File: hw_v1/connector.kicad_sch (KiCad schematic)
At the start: 36 parts, among them J1 Conn_02x24_Counter_Clockwise, J12 Delphi_Sicma_24, J13 Delphi_Sicma_24, J14 Conn_01x04, Q3 FDS6890A, U11 L78M05ABDT-TR, U12 LM74800, U19 L78M05ABDT-TR

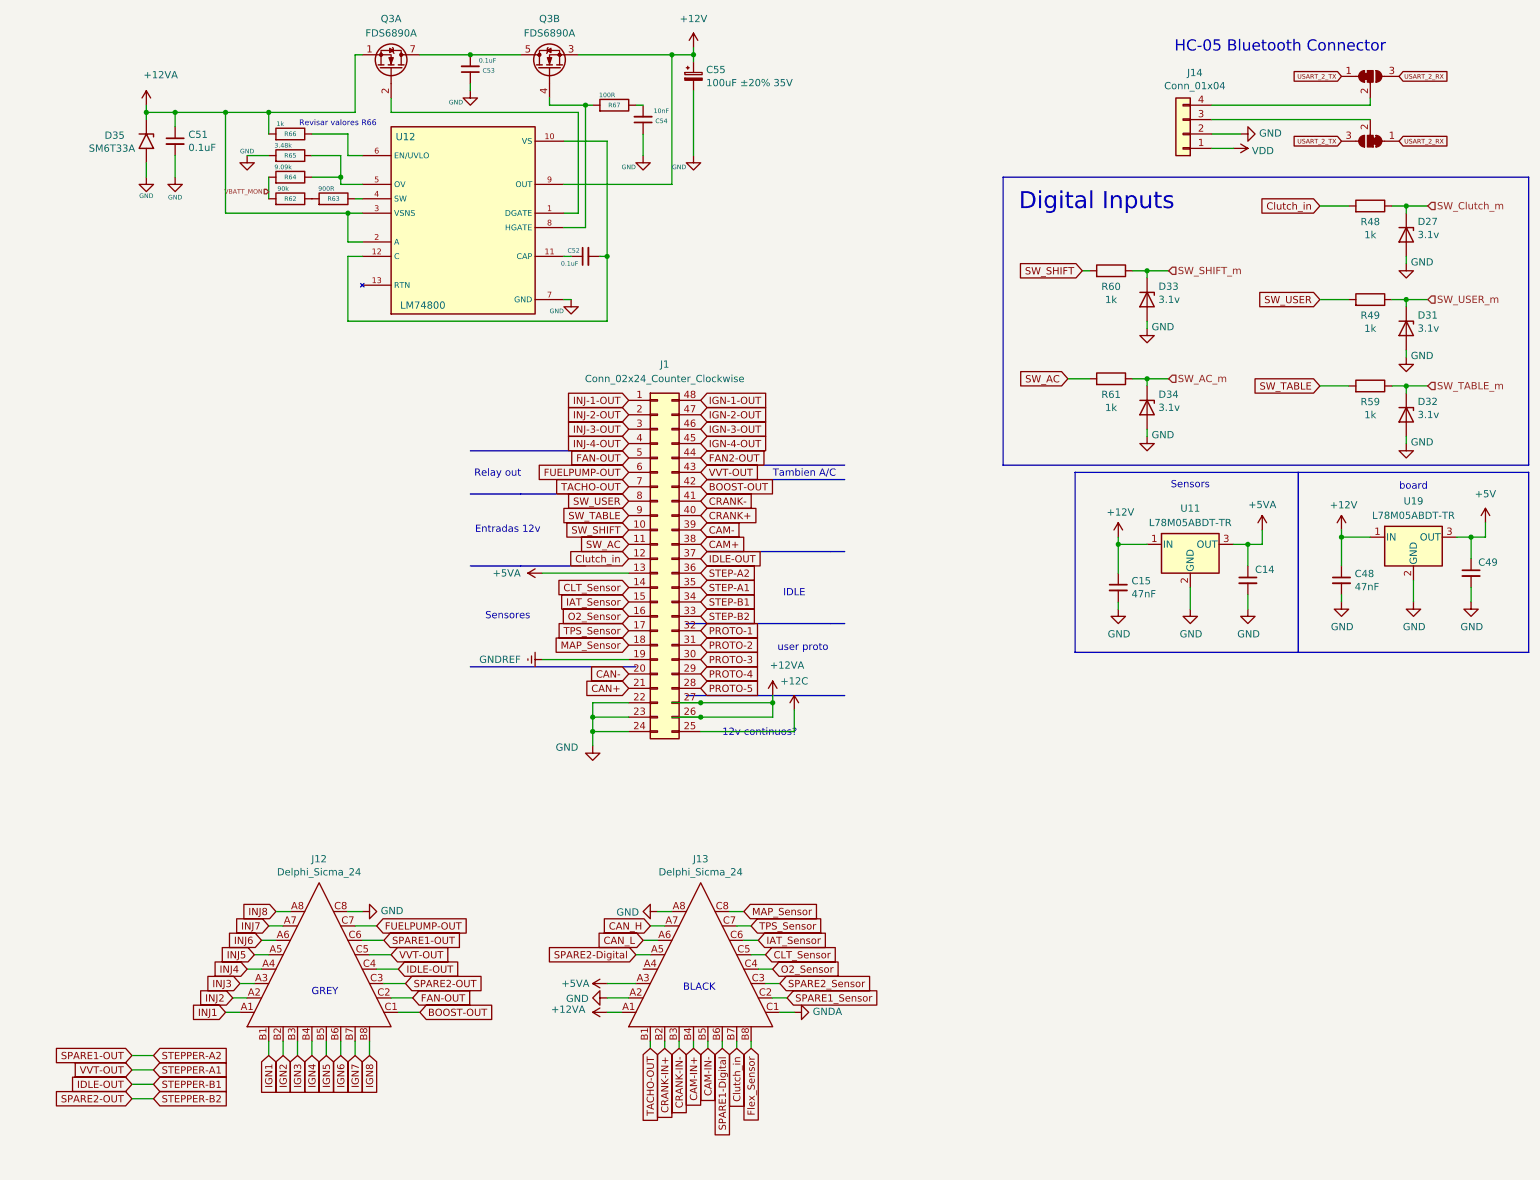
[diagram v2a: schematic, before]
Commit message: wip sensors traces, added can
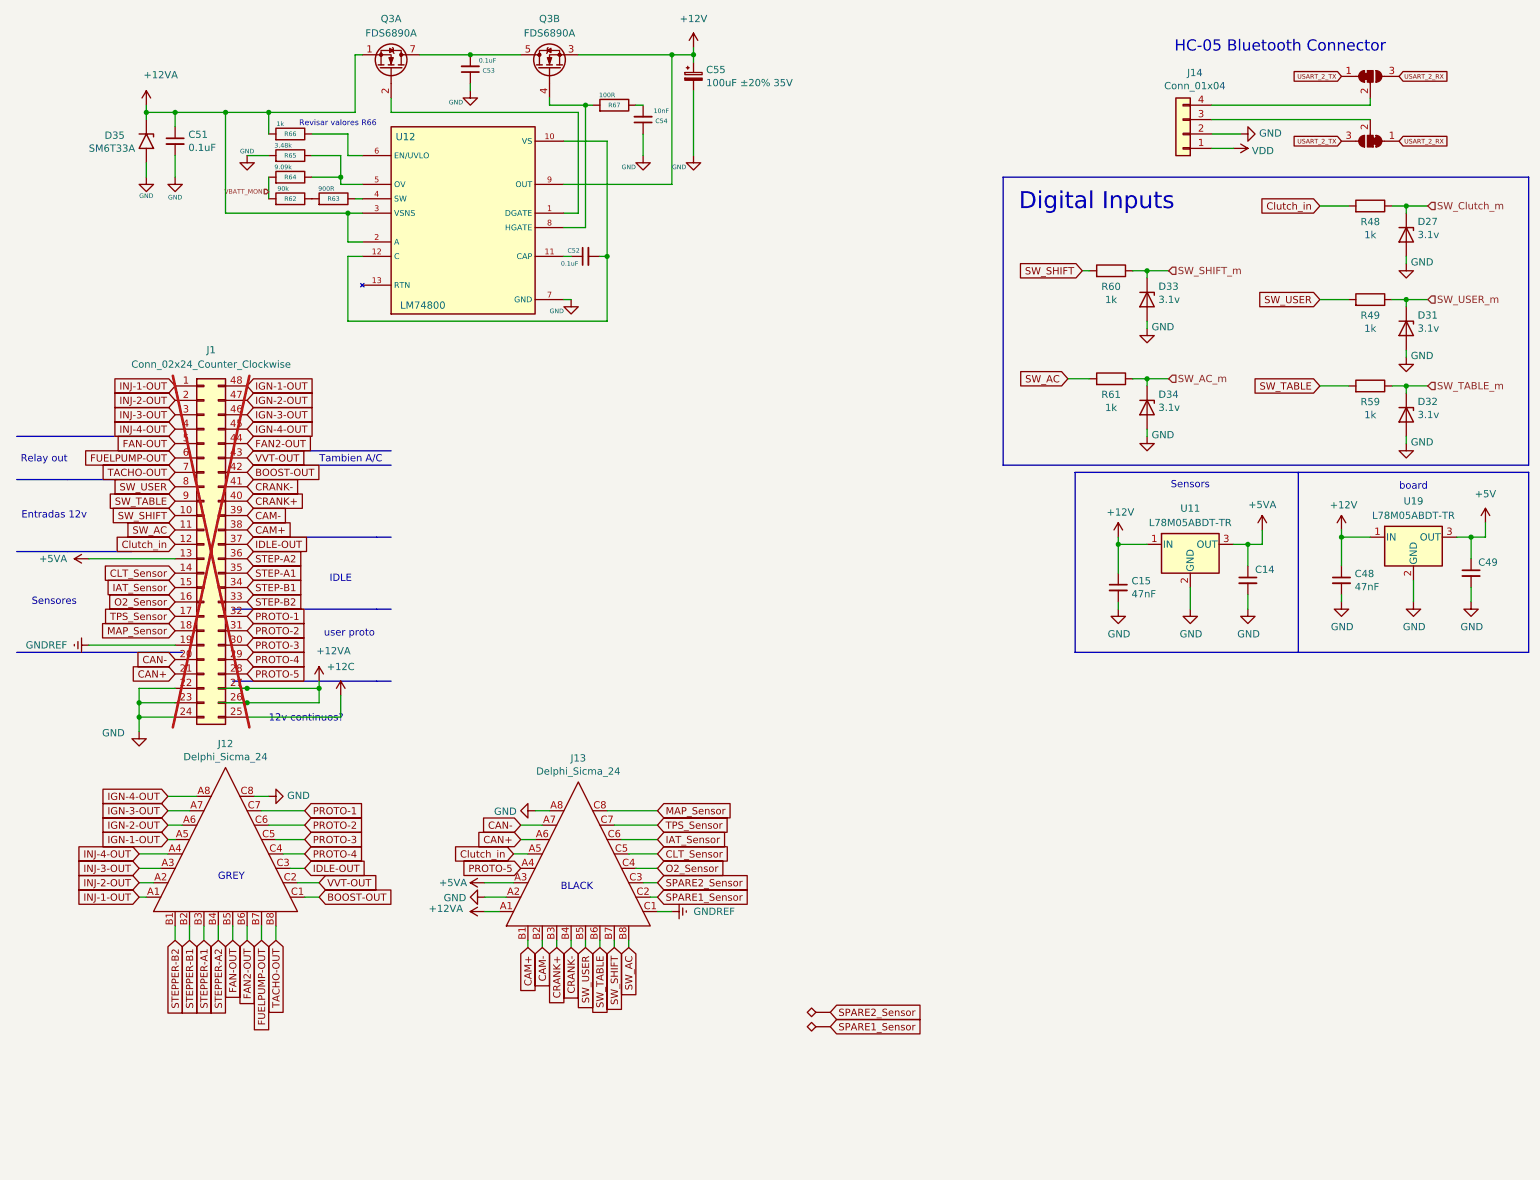
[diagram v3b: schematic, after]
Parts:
- added TP19, TP20: TestPoint_Alt, TestPoint:TestPoint_THTPad_1.0x1.0mm_Drill0.5mm, symbol Connector:TestPoint_Alt
- J1: now not fitted; now left out of the parts list
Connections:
- net CAM-IN+ is gone; now on net CRANK-: J13.B4
- net CAM-IN- is gone; now on net SW_USER: J13.B5
- net CAN_H is gone; now on net CAN-: J13.A7
- net CAN_L is gone; now on net CAN+: J13.A6
- net CRANK-IN+ is gone; now on net CAM-: J13.B2
- net CRANK-IN- is gone; now on net CRANK+: J13.B3
- net Flex_Sensor is gone; now on net SW_AC: J13.B8
- net GNDA is gone; now on net GNDREF: J13.C1
- net IGN3 is gone; now on net STEPPER-A1: J12.B3
- net IGN5 is gone; now on net FAN-OUT: J12.B5
- net IGN6 is gone; now on net FAN2-OUT: J12.B6
- net IGN7 is gone; now on net FUELPUMP-OUT: J12.B7
- net IGN8 is gone; now on net TACHO-OUT: J12.B8
- net INJ1 is gone; now on net INJ-1-OUT: J12.A1
- net INJ2 is gone; now on net INJ-2-OUT: J12.A2
- net INJ3 is gone; now on net INJ-3-OUT: J12.A3
- net INJ4 is gone; now on net INJ-4-OUT: J12.A4
- net INJ5 is gone; now on net IGN-1-OUT: J12.A5
- net INJ6 is gone; now on net IGN-2-OUT: J12.A6
- net INJ7 is gone; now on net IGN-3-OUT: J12.A7
- net INJ8 is gone; now on net IGN-4-OUT: J12.A8
- net SPARE1-Digital is gone; now on net SW_TABLE: J13.B6
- net SPARE1-OUT is gone; now on net PROTO-2: J12.C6
- net SPARE2-Digital is gone; now on net Clutch_in: J13.A5
- net SPARE2-OUT is gone; now on net IDLE-OUT: J12.C3
- net CAM+: now also J13.B1
- net Clutch_in: no longer J13.B7
- net FAN-OUT: no longer J12.C2
- net FUELPUMP-OUT: no longer J12.C7
- net IDLE-OUT: no longer J12.C4
- net PROTO-1: now also J12.C7
- net PROTO-3: now also J12.C5
- net PROTO-4: now also J12.C4
- net PROTO-5: now also J13.A4
- net SPARE1_Sensor: now also TP20.1
- net SPARE2_Sensor: now also TP19.1
- net STEPPER-A1: no longer J1.43 (Pin_43), J12.C5
- net SW_SHIFT: now also J13.B7
- net TACHO-OUT: no longer J13.B1
- net IGN1 renamed STEPPER-B2
- net IGN2 renamed STEPPER-B1
- net IGN4 renamed STEPPER-A2
- new net VVT-OUT: J1.43 (Pin_43), J12.C2
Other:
- moved on the sheet: J12, J13

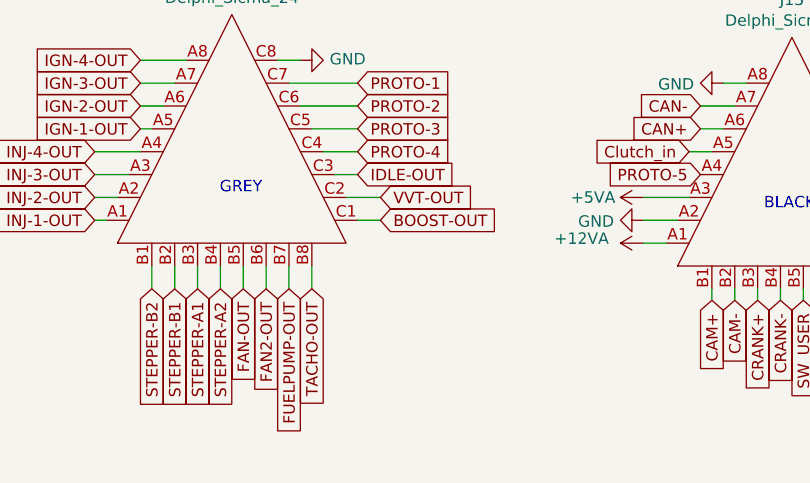
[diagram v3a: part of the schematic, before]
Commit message: ckp/cmp sensor layout
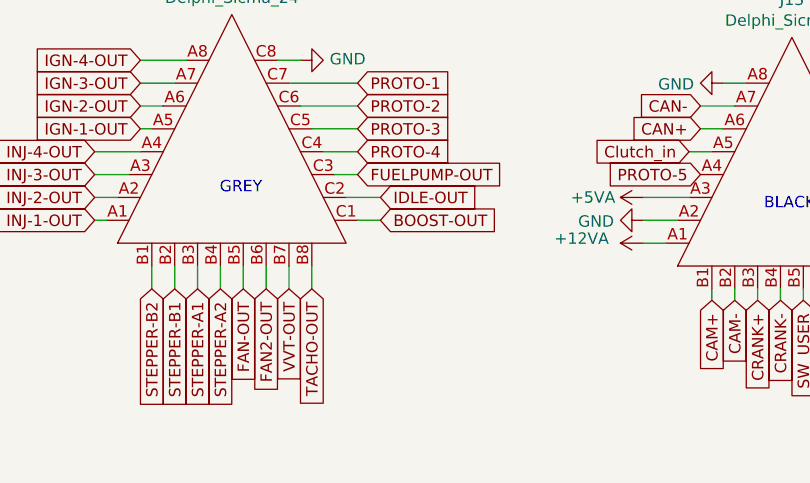
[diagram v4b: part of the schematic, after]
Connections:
- net FUELPUMP-OUT: now also J12.C3; no longer J12.B7
- net IDLE-OUT: now also J12.C2; no longer J12.C3
- net VVT-OUT: now also J12.B7; no longer J12.C2

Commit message: finish pcb layout
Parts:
- added C9: 100nF, Capacitor_SMD:C_0805_2012Metric, symbol Device:C_Small
- added U8: AMS1117-3.3, Package_TO_SOT_SMD:SOT-223-3_TabPin2, symbol Regulator_Linear:AMS1117-3.3
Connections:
- net +5V: now also U8.3 (VI)
- net GND: now also C9.2, U8.1 (GND)
- new net +3V3: C9.1, U8.2 (VO)

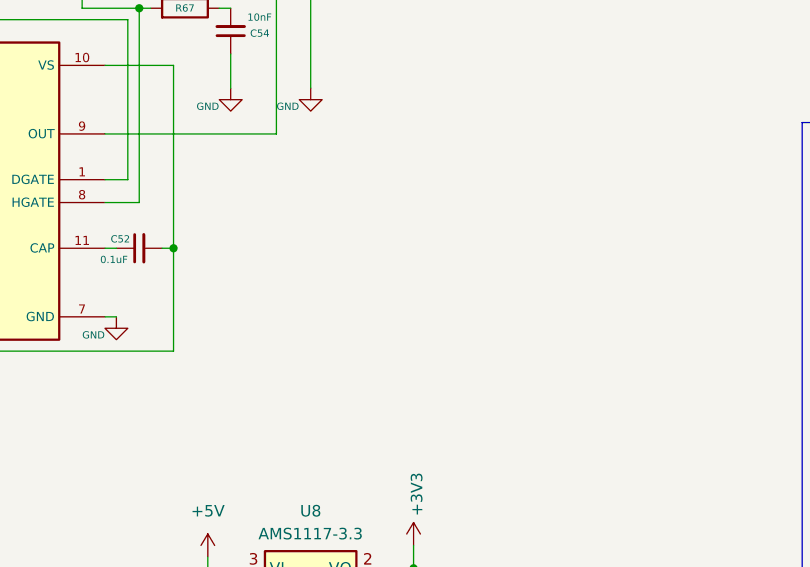
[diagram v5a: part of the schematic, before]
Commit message: update SD card holder to Molex 47352
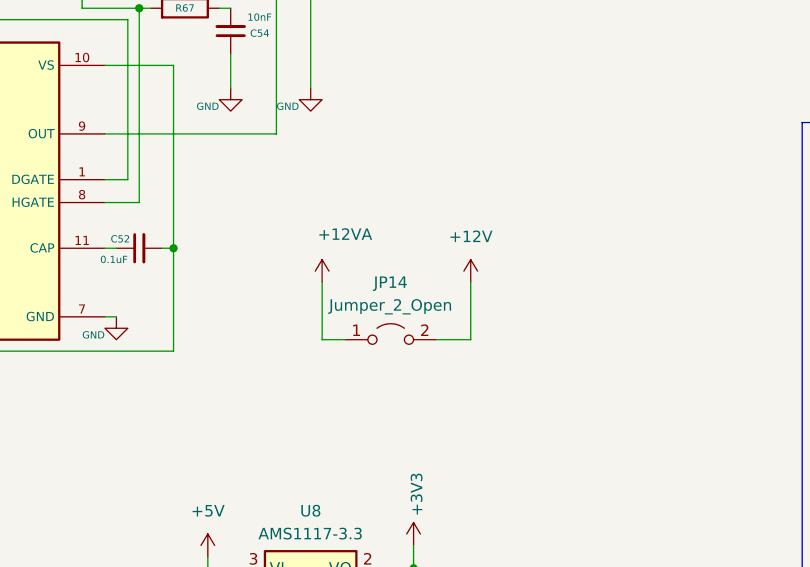
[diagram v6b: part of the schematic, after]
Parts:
- added JP14: Jumper_2_Open, Jumper:SolderJumper-2_P1.3mm_Open_TrianglePad1.0x1.5mm, symbol Jumper:Jumper_2_Open
- J12, J13, JP10, JP9: now left out of the parts list
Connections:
- net +12V: now also JP14.2 (B)
- net +12VA: now also JP14.1 (A)
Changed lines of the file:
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@@
 	(version 20231120)
 	(generator "eeschema")
-	(generator_version "7.99")
+	(generator_version "8.0")
 	(paper "A4")
 	(title_block
 		(title "μEFI (Speeduino FW compatible)")
 		(date "2023-12-25")
-		(rev "v6")
+		(rev "v6.1")
 		(company "Churrosoft ®")
-		(comment 1 "CERN-OHL-S-2.0 license\n")
+		(comment 1 "CERN-OHL-S-2.0 license")
 	)
 	(junction
@@
 	(wire
 		(pts
+			(xy 151.13 62.23) (xy 151.13 68.58)
+		)
+		(stroke
+			(width 0)
+			(type default)
+		)
+	)
+	(wire
+		(pts
 			(xy 213.36 81.28) (xy 213.36 80.01)
 		)
@@
 	(wire
 		(pts
+			(xy 134.62 62.23) (xy 134.62 68.58)
+		)
+		(stroke
+			(width 0)
+			(type default)
+		)
+	)
+	(wire
+		(pts
 			(xy 110.49 45.72) (xy 129.54 45.72)
 		)
@@
 		)
 	)
+	(wire
+		(pts
+			(xy 151.13 68.58) (xy 147.32 68.58)
+		)
+		(stroke
+			(width 0)
+			(type default)
+		)
+	)
 	(polyline
 		(pts
@@
 	(wire
 		(pts
+			(xy 134.62 68.58) (xy 137.16 68.58)
+		)
+		(stroke
+			(width 0)
+			(type default)
+		)
+	)
+	(wire
+		(pts
 			(xy 121.92 180.34) (xy 121.92 179.07)
 		)
@@
 		(unit 1)
 		(exclude_from_sim no)
-		(in_bom yes)
+		(in_bom no)
 		(on_board yes)
 		(dnp no)
@@
 	)
 	(symbol
+		(lib_id "power:+12VA")
+		(at 134.62 62.23 0)
+		(unit 1)
+		(exclude_from_sim no)
+		(in_bom yes)
+		(on_board yes)
+		(dnp no)
+		(property "Reference" "#PWR0175"
+			(at 134.62 66.04 0)
+			(effects
+				(font
+					(size 1.27 1.27)
+				)
+				(hide yes)
+			)
+		)
+		(property "Value" "+12VA"
+			(at 137.16 56.896 0)
+			(effects
+				(font
+					(size 1.27 1.27)
+				)
+			)
+		)
+		(property "Footprint" ""
+			(at 134.62 62.23 0)
+			(effects
+				(font
+					(size 1.27 1.27)
+				)
+				(hide yes)
+			)
+		)
+		(property "Datasheet" ""
+			(at 134.62 62.23 0)
+			(effects
+				(font
+					(size 1.27 1.27)
+				)
+				(hide yes)
+			)
+		)
+		(property "Description" "Power symbol creates a global label with name \"+12VA\""
+			(at 134.62 62.23 0)
+			(effects
+				(font
+					(size 1.27 1.27)
+				)
+				(hide yes)
+			)
+		)
+		(pin "1"
+		)
+		(instances
+			(project "hw_v1"
+				(path "/b3feb07e-be80-40e1-bd13-6cd54c2f8b0c/312f3a58-86c6-4c57-9da0-ed62046efef3"
+					(reference "#PWR0175")
+					(unit 1)
+				)
+			)
+		)
+	)
+	(symbol
 		(lib_id "Connector_Generic:Conn_02x24_Counter_Clockwise")
 		(at 46.99 109.22 0)
@@
 		(unit 1)
 		(exclude_from_sim no)
-		(in_bom yes)
+		(in_bom no)
 		(on_board yes)
 		(dnp no)
@@
 		(unit 1)
 		(exclude_from_sim no)
-		(in_bom yes)
+		(in_bom no)
 		(on_board yes)
 		(dnp no)
@@
 	)
 	(symbol
+		(lib_name "+12V_1")
+		(lib_id "power:+12V")
+		(at 151.13 62.23 0)
+		(unit 1)
+		(exclude_from_sim no)
+		(in_bom yes)
+		(on_board yes)
+		(dnp no)
+		(fields_autoplaced yes)
+		(property "Reference" "#PWR0176"
+			(at 151.13 66.04 0)
+			(effects
+				(font
+					(size 1.27 1.27)
+				)
+				(hide yes)
+			)
+		)
+		(property "Value" "+12V"
+			(at 151.13 57.15 0)
+			(effects
+				(font
+					(size 1.27 1.27)
+				)
+			)
+		)
+		(property "Footprint" ""
+			(at 151.13 62.23 0)
+			(effects
+				(font
+					(size 1.27 1.27)
+				)
+				(hide yes)
+			)
+		)
+		(property "Datasheet" ""
+			(at 151.13 62.23 0)
+			(effects
+				(font
+					(size 1.27 1.27)
+				)
+				(hide yes)
+			)
+		)
+		(property "Description" "Power symbol creates a global label with name \"+12V\""
+			(at 151.13 62.23 0)
+			(effects
+				(font
+					(size 1.27 1.27)
+				)
+				(hide yes)
+			)
+		)
+		(pin "1"
+		)
+		(instances
+			(project "hw_v1"
+				(path "/b3feb07e-be80-40e1-bd13-6cd54c2f8b0c/312f3a58-86c6-4c57-9da0-ed62046efef3"
+					(reference "#PWR0176")
+					(unit 1)
+				)
+			)
+		)
+	)
+	(symbol
 		(lib_id "Device:C_Small")
 		(at 124.46 34.29 180)
@@
 	)
 	(symbol
+		(lib_id "Jumper:Jumper_2_Open")
+		(at 142.24 68.58 0)
+		(unit 1)
+		(exclude_from_sim no)
+		(in_bom yes)
+		(on_board yes)
+		(dnp no)
+		(fields_autoplaced yes)
+		(property "Reference" "JP14"
+			(at 142.24 62.23 0)
+			(effects
+				(font
+					(size 1.27 1.27)
+				)
+			)
+		)
+		(property "Value" "Jumper_2_Open"
+			(at 142.24 64.77 0)
+			(effects
+				(font
+					(size 1.27 1.27)
+				)
+			)
+		)
+		(property "Footprint" "Jumper:SolderJumper-2_P1.3mm_Open_TrianglePad1.0x1.5mm"
+			(at 142.24 68.58 0)
+			(effects
+				(font
+					(size 1.27 1.27)
+				)
+				(hide yes)
+			)
+		)
+		(property "Datasheet" "~"
+			(at 142.24 68.58 0)
+			(effects
+				(font
+					(size 1.27 1.27)
+				)
+				(hide yes)
+			)
+		)
+		(property "Description" "Jumper, 2-pole, open"
+			(at 142.24 68.58 0)
+			(effects
+				(font
+					(size 1.27 1.27)
+				)
+				(hide yes)
+			)
+		)
+		(pin "1"
+		)
+		(pin "2"
+		)
+		(instances
+			(project "hw_v1"
+				(path "/b3feb07e-be80-40e1-bd13-6cd54c2f8b0c/312f3a58-86c6-4c57-9da0-ed62046efef3"
+					(reference "JP14")
+					(unit 1)
+				)
+			)
+		)
+	)
+	(symbol
 		(lib_id "power:GND")
 		(at 93.98 29.21 0)
@@
 		(unit 1)
 		(exclude_from_sim no)
-		(in_bom yes)
+		(in_bom no)
 		(on_board yes)
 		(dnp no)

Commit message: update vr inputs
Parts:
- JP14: now left out of the parts list
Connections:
- net PROTO-5 renamed CEL-OUT
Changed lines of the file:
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@@
 	(wire
 		(pts
+			(xy 86.36 162.56) (xy 86.36 166.37)
+		)
+		(stroke
+			(width 0)
+			(type default)
+		)
+	)
+	(wire
+		(pts
 			(xy 35.56 139.7) (xy 35.56 137.16)
 		)
@@
 	(wire
 		(pts
+			(xy 86.36 166.37) (xy 102.87 166.37)
+		)
+		(stroke
+			(width 0)
+			(type default)
+		)
+	)
+	(wire
+		(pts
 			(xy 208.28 119.38) (xy 208.28 120.65)
 		)
@@
 		)
 	)
+	(global_label "CEL-OUT"
+		(shape input)
+		(at 86.36 162.56 90)
+		(effects
+			(font
+				(size 1.27 1.27)
+			)
+			(justify left)
+		)
+		(property "Intersheetrefs" "${INTERSHEET_REFS}"
+			(at 86.36 162.56 0)
+			(effects
+				(font
+					(size 1.27 1.27)
+				)
+				(hide yes)
+			)
+		)
+	)
 	(global_label "STEP-B2"
 		(shape input)
@@
 	(global_label "PROTO-5"
 		(shape input)
-		(at 102.87 166.37 180)
+		(at 93.98 166.37 180)
 		(effects
 			(font
@@
 		)
 		(property "Intersheetrefs" "${INTERSHEET_REFS}"
-			(at 102.87 166.37 0)
+			(at 93.98 166.37 0)
 			(effects
 				(font
@@
 		(unit 1)
 		(exclude_from_sim no)
-		(in_bom yes)
+		(in_bom no)
 		(on_board yes)
 		(dnp no)

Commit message: wip inventree updates
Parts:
- R62: value 90k -> 48.7k
- R63: value 900R -> 42.2k
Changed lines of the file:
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@@
 			)
 		)
-		(property "Value" "90k"
+		(property "Value" "48.7k"
 			(at 60.96 46.482 90)
 			(effects
@@
 			)
 		)
-		(property "Value" "900R"
+		(property "Value" "42.2k"
 			(at 68.58 46.482 90)
 			(effects
